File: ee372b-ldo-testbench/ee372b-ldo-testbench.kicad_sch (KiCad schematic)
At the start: 87 parts, among them J1 PEC02SAAN, J10 OUT_S, J11 VOUT, J12 VDD_BUF, J13 V_SIG, J15 VSIG_BUF, J2 PEC02SAAN, J3 PEC02SAAN, J4 PEC02SAAN, J5 VOUT, J6 GND, J7 PEC02SAAN, J8 VIN, J9 IN_S, Q1 FDV305N, Q2 FDV305N, Q3 FDV305N, Q4 FDV305N, Q5 FDV305N, U3 ADS1220IPW, U4 BUF634AIDR

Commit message: finished initial testbench?
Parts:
- removed J1, J2, J3, J4, J7: PEC02SAAN, switched_R_Load_footprints_lib:CONN_PxC02S_SUL, symbol switched_R_load_symlib:PEC02SAAN
- added A1: RaspberryPi_Pico, Module:RaspberryPi_Pico_Common_Unspecified, symbol MCU_Module:RaspberryPi_Pico
- added C1, C14, C15, C16, C2, C3: 0.1uF, symbol Device:C
- added C12, C8: 1uF, symbol Device:C
- added J14, J16, J17, J18, J19: PEC03SAAN, CONN_PEC03SAAN_SUL, symbol 1_EE372_LDO:PEC03SAAN
- added J20: VREF_EXTERNAL, SMA_J_P_H_ST_TH1:SAMTEC_SMA-J-P-H-ST-TH1, symbol SMA-J-P-H-ST-TH1:SMA-J-P-H-ST-TH1
- added J3: GND, CALTEST_CT3151-2:CALTEST_CT3151-2, symbol Connector:Conn_01x01_Pin
- added J4: 1V8, CALTEST_CT3151-2:CALTEST_CT3151-2, symbol Connector:Conn_01x01_Pin
- added R1, R2, R3, R4, R5: 47, symbol Device:R
- added R57, R58, R60: 0, symbol Device:R
- added R6, R7, R8: 1k, symbol Device:R
- added TP5: OTA_OUT, Keystone 5016 testpoint:KEYSTONE_5016, symbol Connector:TestPoint
- added TP6: GND, Keystone 5016 testpoint:KEYSTONE_5016, symbol Connector:TestPoint
- added TP7: 1V8, Keystone 5016 testpoint:KEYSTONE_5016, symbol Connector:TestPoint
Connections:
- net BGR_VREF: now also R48.1, R57.2; no longer R37.1
- net GND: now also R21.2, R22.2, R23.2, R24.2, R25.2, R26.2, R27.2, R28.2, R29.2, R30.2, R31.2, R32.2, R33.2, R34.2, R35.2, R36.2, U3.3 (CLK), U3.4 (DGND), U3.5 (AVSS), C1.2, C12.2, C14.2, C15.2, C16.2, C2.2, C8.2, J20.G1, J20.G2, J20.G3, J20.G4, J3.1 (Pin_1), J4.1 (Pin_1), TP6.1, TP7.1
- net LDO_VOUT: now also R50.1, R51.1, R53.1
- net VG0: now also J14.2
- net VG1: now also J16.2
- net VG2: now also J17.2
- net VG3: now also J18.2
- net VG4: now also J19.2
- net VIN: no longer J5.1 (Pin_1), R11.1, R13.1, R16.1, R18.1, R19.1, R20.1
- net VOUT: now also J5.1 (Pin_1), R11.1, R13.1, R16.1, R18.1, R19.1, R20.1
- net 1V8: now reaches R46.2
- net 1V8: now also C4.1, C5.1, C6.1, R39.2, R40.2, R41.2, R42.2, R43.2, R44.2, R45.2, R47.2, R56.2, TP2.1
- net at R49.1: now also TP5.1
- net at R49.2, U2.15 (OTA_OUT): now also R58.2
- net at R37.2, U2.19 (OTA_VREF): now also R57.1
- net at R48.2, U2.5 (BGR_VREF): now also R60.2
- net at U3.1 (SCLK): now also R2.2
- net AIN1_ADC: now reaches U3.10 (AIN1)
- net AIN1_ADC: now also C16.1, R8.2
- net AIN0_ADC: now reaches U3.11 (AIN0/REFP1)
- net AIN0_ADC: now also C14.1, R6.2
- net 3V3: now reaches U3.12 (AVDD)
- net 3V3: now also U3.13 (DVDD), A1.36 (3V3), C1.1, C12.1, C2.1, C3.2, C8.1, J14.1, J16.1, J17.1, J18.1, J19.1
- net at U3.14 (*DRDY): now also R4.2
- net at U3.15 (DOUT/*DRDY): now also R3.1
- net at U3.16 (DIN): now also R5.2
- net at U3.2 (*CS): now also R1.1
- net AIN3_ADC: now reaches U3.6 (AIN3/REFN1)
- net AIN2_ADC: now reaches U3.7 (AIN2)
- net AIN2_ADC: now also C15.1, R7.2
- new net: A1.13 (GND), A1.18 (GND), A1.23 (GND), A1.28 (GND), A1.3 (GND), A1.38 (GND), A1.8 (GND), C3.1
- new net: J20.1, R37.1
- new net AIN0_SIGNAL: R6.1
- new net AIN1_SIGNAL: R60.1, R8.1
- new net AIN2_SIGNAL: R58.1, R7.1
- new net pico_irq: A1.9 (GPIO6), R4.1
- new net pico_spi_clk: A1.4 (GPIO2), R2.1
- new net pico_spi_cs: A1.2 (GPIO1), R1.2
- new net pico_spi_rx: A1.6 (GPIO4), R3.2
- new net pico_spi_tx: A1.5 (GPIO3), R5.1
- new net pico_vg0: A1.14 (GPIO10), J14.3
- new net pico_vg1: A1.15 (GPIO11), J16.3
- new net pico_vg2: A1.16 (GPIO12), J17.3
- new net pico_vg3: A1.17 (GPIO13), J18.3
- new net pico_vg4: A1.19 (GPIO14), J19.3
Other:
- note added: "Banana jacks for VDD/GND"
- moved on the sheet: R37, R48, R49, U3

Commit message: add MMSZ4679T1G zener diode symbol, footprint
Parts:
- removed C10, C4: 10uF, Capacitor_SMD:C_0805_2012Metric_Pad1.18x1.45mm_HandSolder, symbol Device:C
- removed C5, C9: 100nF, Capacitor_SMD:C_0805_2012Metric_Pad1.18x1.45mm_HandSolder, symbol Device:C
- removed C6, C7: 0.1nF, Capacitor_SMD:C_0805_2012Metric_Pad1.18x1.45mm_HandSolder, symbol Device:C
- added C17, C22: 10uF, Capacitor_SMD:C_0805_2012Metric_Pad1.18x1.45mm_HandSolder, symbol Device:C
- added C18, C21: 100nF, Capacitor_SMD:C_0805_2012Metric_Pad1.18x1.45mm_HandSolder, symbol Device:C
- added C19, C20: 0.1nF, Capacitor_SMD:C_0805_2012Metric_Pad1.18x1.45mm_HandSolder, symbol Device:C
- added J1, J2, J21, J22, J23, J7: PEC02SAAN, CONN_PxC02S_SUL, symbol 1_EE372_DemoBoard:PEC02SAAN
- added R61, R9: R, symbol Device:R
- added R62: 0, Resistor_SMD:R_0805_2012Metric_Pad1.20x1.40mm_HandSolder, symbol Device:R
- R38: value 0 -> R
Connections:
- net 1V8: now also J1.1, J2.1, J7.1; no longer R40.2, R41.2, R42.2, R43.2, R44.2, R45.2, R46.2, R47.2
- net GND: now also C17.2, C18.2, C19.2, C20.2, C21.2, C22.2
- net LDO_VOUT: now also R38.1, R61.1, R9.1
- net VSIG_BUF: now also R62.1; no longer J15.1
- net at U2.33 (EP): no longer R38.1
- net at R38.2: now also J22.1
- new net: J23.1, R61.2
- new net: C20.1, J21.2
- new net: C21.1, J22.2
- new net: C18.1, J2.2
- new net: J15.1, R62.2
- new net: C22.1, J23.2
- new net: C17.1, J7.2
- new net: J21.1, R9.2
- new net: C19.1, J1.2
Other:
- note added: "Selectable Cin and Cout"
- note removed: "C_LOAD capacitors"
- moved on the sheet: A1, C1, C11, C12, C13, C14, C15, C16, C2, C3, C8, H1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

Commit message: passes ERC
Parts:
- added U1: MMSZ4679T1G, SOD-123_ONS, symbol 1_EE372_LDO:MMSZ4679T1G
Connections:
- net 1V8: now also R40.2, R41.2, R42.2, R43.2, R44.2, R45.2, R46.2, R47.2
- net GND: now also U1.2 (ANODE)
- net VIN: now also U1.1 (CATHODE)
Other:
- note added: "2V zener diode overvoltage protection"
- moved on the sheet: J8

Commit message: passes ERC, all footprints assigned
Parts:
- C1, C12, C14, C15, C16, C2, C3, C8: footprint (none) -> Capacitor_SMD:C_0805_2012Metric_Pad1.18x1.45mm_HandSolder
- C11: footprint TPS7A7001_Evaluation_Board_footprint_lib:CAPPRD350W60D800H1150 -> 1_EE372_DemoBoard:CAPPRD350W60D800H1150
- J1, J2, J21, J22, J23, J7: footprint CONN_PxC02S_SUL -> 1_EE372_DemoBoard:CONN_PxC02S_SUL
- J10, J13, J9: footprint TPS7A7001_Evaluation_Board_footprint_lib:SAMTEC_SMA-J-P-H-ST-TH1 -> 1_EE372_DemoBoard:SAMTEC_SMA-J-P-H-ST-TH1
- J11, J12, J3, J4, J8: footprint CALTEST_CT3151-2:CALTEST_CT3151-2 -> 1_EE372_DemoBoard:CALTEST_CT3151-2
- J14, J16, J17, J18, J19: footprint CONN_PEC03SAAN_SUL -> 1_EE372_DemoBoard:CONN_PEC03SAAN_SUL
- J15, J20: footprint SMA_J_P_H_ST_TH1:SAMTEC_SMA-J-P-H-ST-TH1 -> 1_EE372_DemoBoard:SAMTEC_SMA-J-P-H-ST-TH1
- J5, J6: footprint switched_R_Load_footprints_lib:CALTEST_CT3151-2 -> 1_EE372_DemoBoard:CALTEST_CT3151-2
- JP3: footprint TPS7A7001_Evaluation_Board_footprint_lib:CONN_PxC02S_SUL -> 1_EE372_DemoBoard:CONN_PxC02S_SUL
- Q1, Q2, Q3, Q4, Q5: footprint FDV305N:SOT95P240X111-3N -> 1_EE372_DemoBoard:SOT95P240X111-3N
- R1, R2, R21, R22, R23, R24, R25, R26, R27, R28, R29, R3, R30, R31, R32, R33, R34, R35, R36, R37, R39, R4, R40, R41, R42, R43, R44, R45, R46, R47, R48, R49, R5, R50, R51, R52, R53, R57, R58, R6, R60, R7, R8: footprint (none) -> Resistor_SMD:R_0805_2012Metric_Pad1.20x1.40mm_HandSolder
- R38, R61, R9: value R -> 0; footprint (none) -> Resistor_SMD:R_0805_2012Metric_Pad1.20x1.40mm_HandSolder
- TP1, TP2, TP3, TP4, TP5, TP6, TP7: footprint Keystone 5016 testpoint:KEYSTONE_5016 -> 1_EE372_DemoBoard:KEYSTONE_5016
- U2: footprint (none) -> 1_EE372_Quick-Pak:QFN-32_EP_7x7_Pitch0.65mm
- U4: footprint TPS7A7001_Evaluation_Board_footprint_lib:SOIC127P599X175-8N -> 1_EE372_DemoBoard:SOIC127P599X175-8N
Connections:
- net AIN3_ADC is gone; now on net GND: U3.6 (AIN3/REFN1)
- no-connect marks 0 -> 24
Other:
- moved on the sheet: R21, R22, R23, R24, R25, R26, R27, R28, R29, R30, R31, R32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

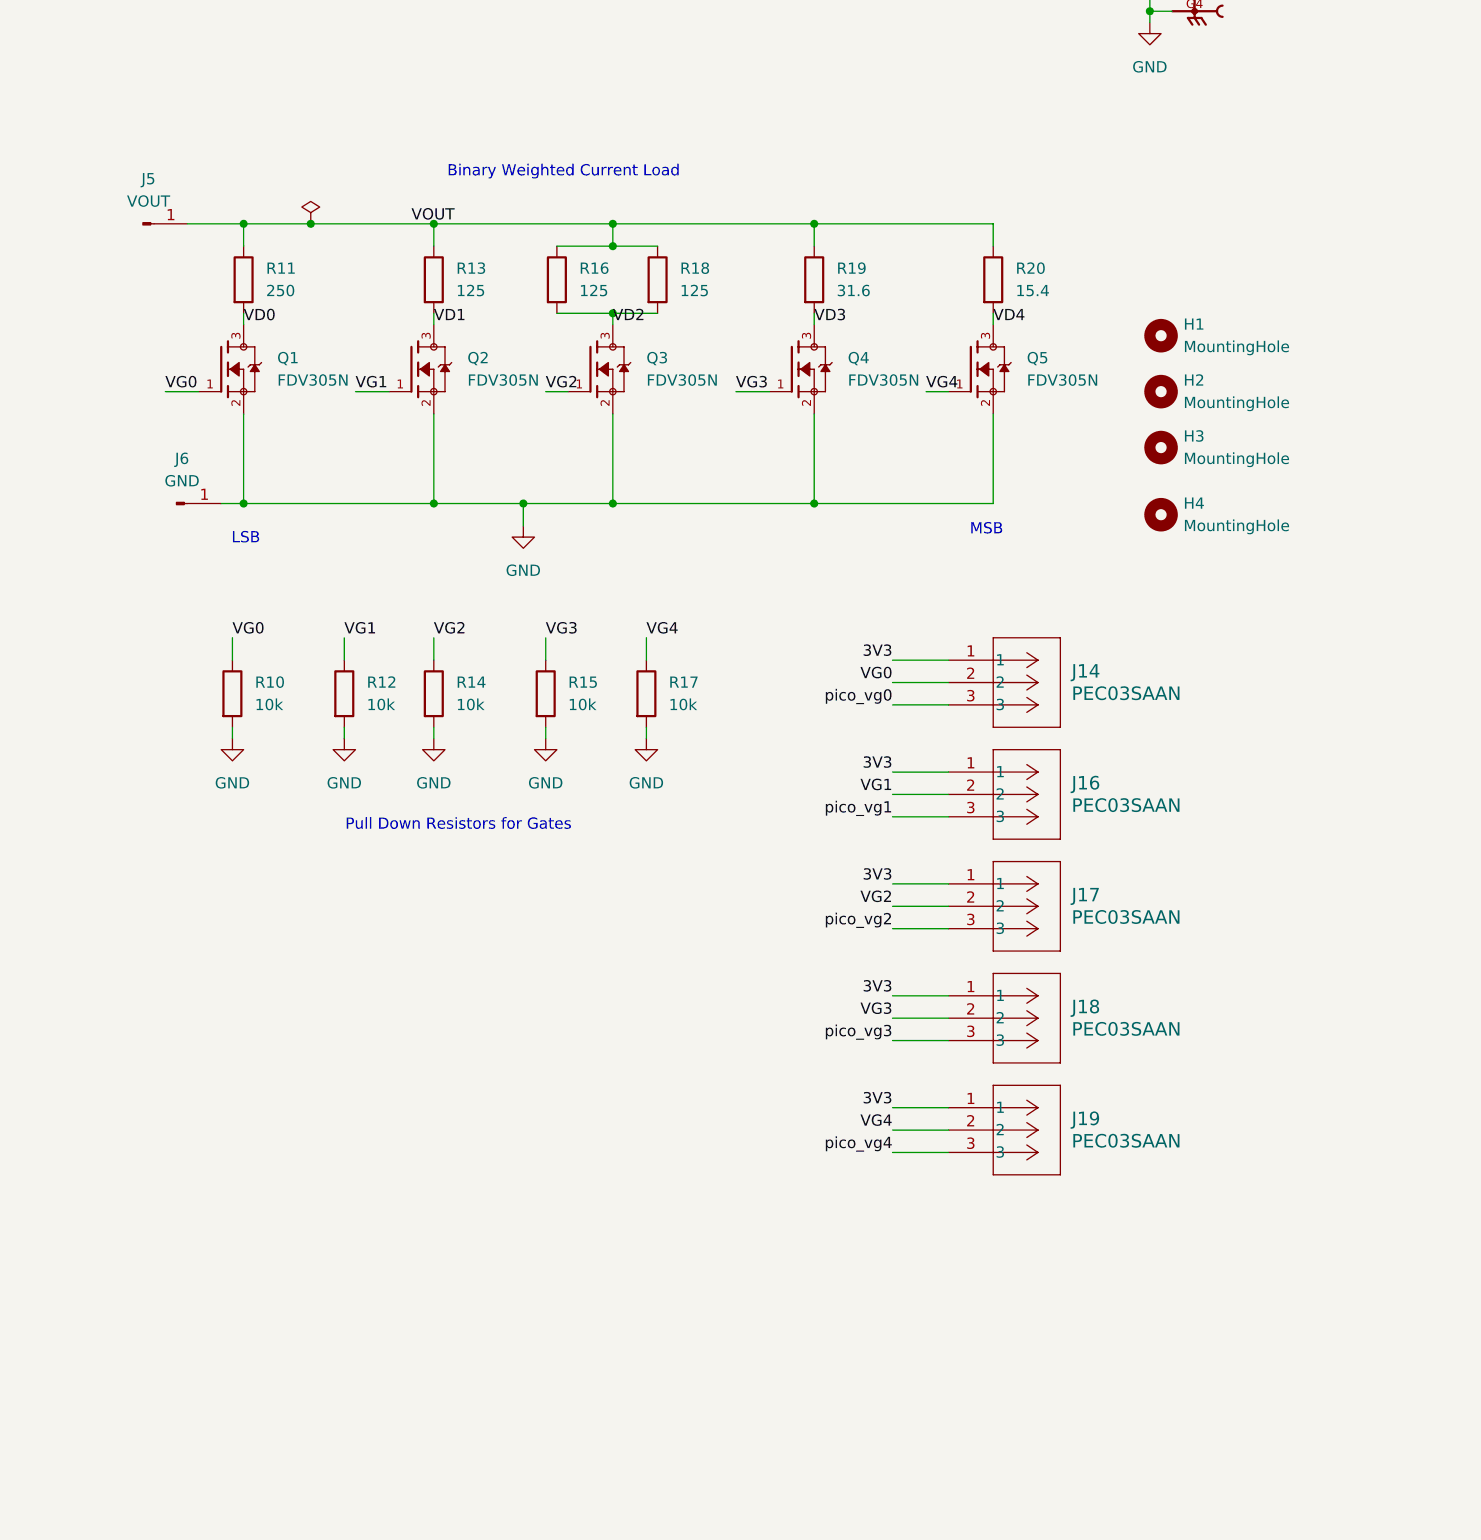
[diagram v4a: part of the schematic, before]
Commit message: updated pcb layout settings to 4 layers
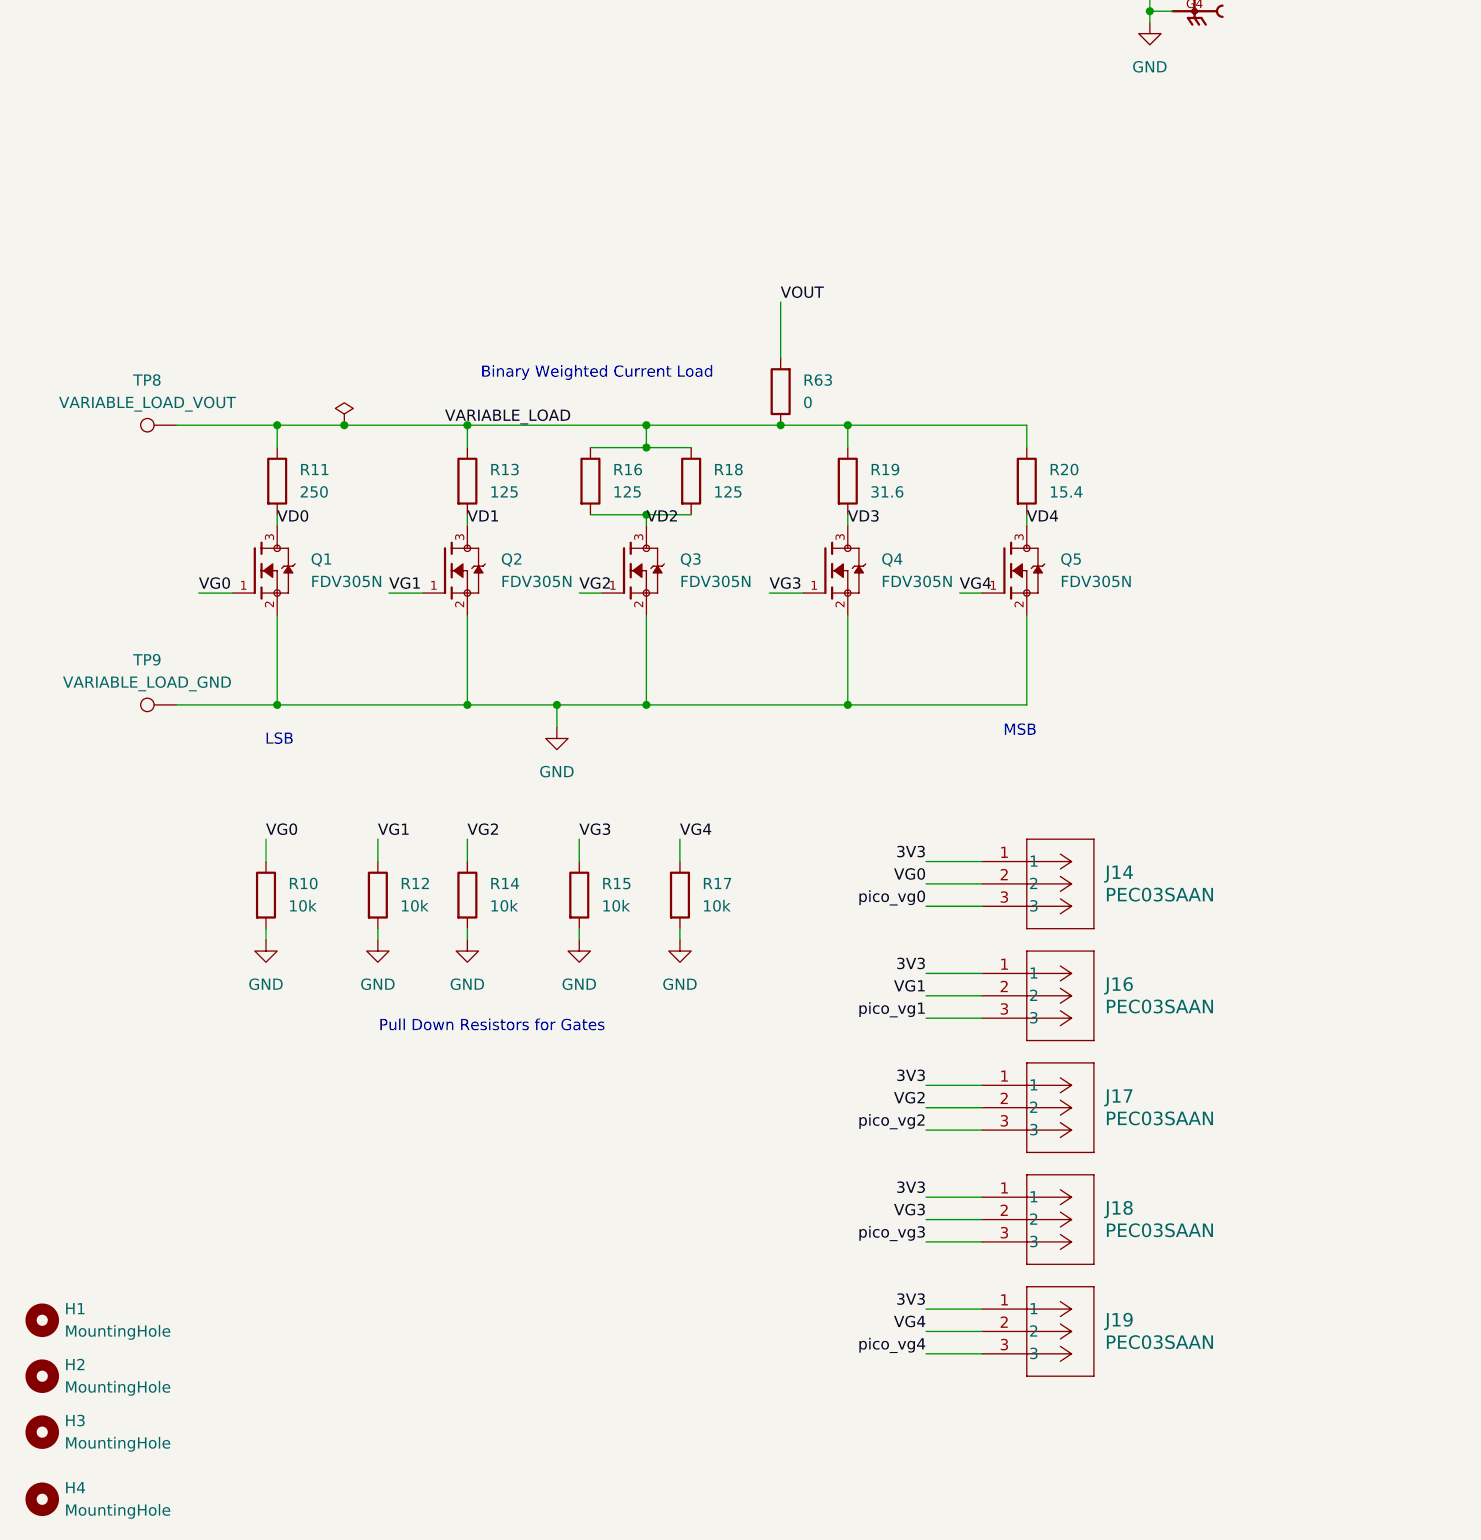
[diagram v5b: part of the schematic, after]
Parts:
- removed J5: VOUT, 1_EE372_DemoBoard:CALTEST_CT3151-2, symbol switched_R_load_symlib:Conn_01x01_Banana_Jack
- removed J6: GND, 1_EE372_DemoBoard:CALTEST_CT3151-2, symbol switched_R_load_symlib:Conn_01x01_Banana_Jack
- added R63: 0, Resistor_SMD:R_0805_2012Metric_Pad1.20x1.40mm_HandSolder, symbol Device:R
- added TP8: VARIABLE_LOAD_VOUT, 1_EE372_DemoBoard:KEYSTONE_5016, symbol Connector:TestPoint
- added TP9: VARIABLE_LOAD_GND, 1_EE372_DemoBoard:KEYSTONE_5016, symbol Connector:TestPoint
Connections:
- net GND: now also TP9.1
- net VOUT: now also R63.2; no longer R11.1, R13.1, R16.1, R18.1, R19.1, R20.1
- new net VARIABLE_LOAD: R11.1, R13.1, R16.1, R18.1, R19.1, R20.1, R63.1, TP8.1
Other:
- moved on the sheet: H1, H2, H3, H4, J14, J16, J17, J18, J19, Q1, Q2, Q3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

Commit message: tweaks to schematic, more bypass caps, ext 3v3 source
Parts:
- removed C17: 10uF, Capacitor_SMD:C_0805_2012Metric_Pad1.18x1.45mm_HandSolder, symbol Device:C
- removed J7: PEC02SAAN, 1_EE372_DemoBoard:CONN_PxC02S_SUL, symbol 1_EE372_DemoBoard:PEC02SAAN
- removed R45, R46, R47: 0, Resistor_SMD:R_0805_2012Metric_Pad1.20x1.40mm_HandSolder, symbol Device:R
- added C10, C17, C23, C24, C4, C5, C6, C7, C9: 100nF, symbol Device:C_Small_US
- added C25: 1uF, Capacitor_SMD:C_0805_2012Metric_Pad1.18x1.45mm_HandSolder, symbol Device:C
- added C26, C28: 10uF, symbol Device:C_Small_US
- added C27: 1uF, symbol Device:C_Small_US
- added J24: PEC02SAAN, 1_EE372_DemoBoard:CONN_PxC02S_SUL, symbol 1_EE372_DemoBoard:PEC02SAAN
- added J25: PEC03SAAN, 1_EE372_DemoBoard:CONN_PEC03SAAN_SUL, symbol 1_EE372_LDO:PEC03SAAN
- added J5: 3v3_EXTERNAL, 1_EE372_DemoBoard:CALTEST_CT3151-2, symbol Connector:Conn_01x01_Pin
- added TP10: 1V8, 1_EE372_DemoBoard:KEYSTONE_5016, symbol Connector:TestPoint
- C18: value 100nF -> 1uF
- C19: value 0.1nF -> 10nF
- C20: value 0.1nF -> 1nF
- R44: value 0 -> R; footprint Resistor_SMD:R_0805_2012Metric_Pad1.20x1.40mm_HandSolder -> (none)
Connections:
- net 3V3: now also J25.2; no longer A1.36 (3V3), C3.2
- net GND: now also R39.1, R40.1, R41.1, R43.1, C10.1, C17.1, C23.1, C24.1, C25.2, C26.2, C27.1, C28.2, C4.1, C5.1, C6.1, C7.1, C9.1; no longer J4.1 (Pin_1), TP7.1
- net LDO_VOUT: now also R42.1
- net at C20.1, J21.2: now also R41.2
- net at C21.1, J22.2: now also R39.2
- net at U2.27 (VDD): now also C23.2
- net at U2.16 (VDD): now also C7.2; no longer R42.1
- net at C22.1, J23.2: now also R40.2
- net at U2.32 (VDD): now also C24.2, C27.2
- net c1_vin_jump: now reaches U2.2 (VDD)
- net c1_vin_jump: now also J1.1, J2.1, R56.2, TP2.1, C4.2; no longer R39.1
- net at U2.17 (VDD): now also C9.2; no longer R43.1
- net at U2.14 (VDD): now also C6.2; no longer R41.1
- net at R44.1: now also J25.3; no longer U2.21 (VDD)
- net at U2.24 (VDD): now also C17.2
- net at U2.8 (VDD): now also C5.2; no longer R40.1
- removed net 1V8: J1.1, J2.1, R39.2, R40.2, R41.2, R42.2, R43.2, R44.2, R56.2, TP2.1
- new net: C25.1, J24.2, R43.2
- new net: C26.1, J4.1 (Pin_1), TP7.1
- new net: C28.1, J5.1 (Pin_1), TP10.1
- new net: J24.1, R42.2
- new net: C10.2, U2.21 (VDD)
- new net 3V3_EXTERNAL: J25.1
- new net 3V3_PICO: A1.36 (3V3), C3.2, R44.2
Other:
- moved on the sheet: C20, C21, C22, J23, R55, R61
